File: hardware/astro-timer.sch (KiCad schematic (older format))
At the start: 25 parts, among them J1 Conn_01x02_Male, J2 AVR-ISP-6, J3 AudioJack2, SW1 SW_SPST, SW2 SW_Push, SW3 SW_Push, SW4 Rotary_Encoder_Switch, U1 ATmega328P-PU, U2 LTV-817M, Y1 Crystal

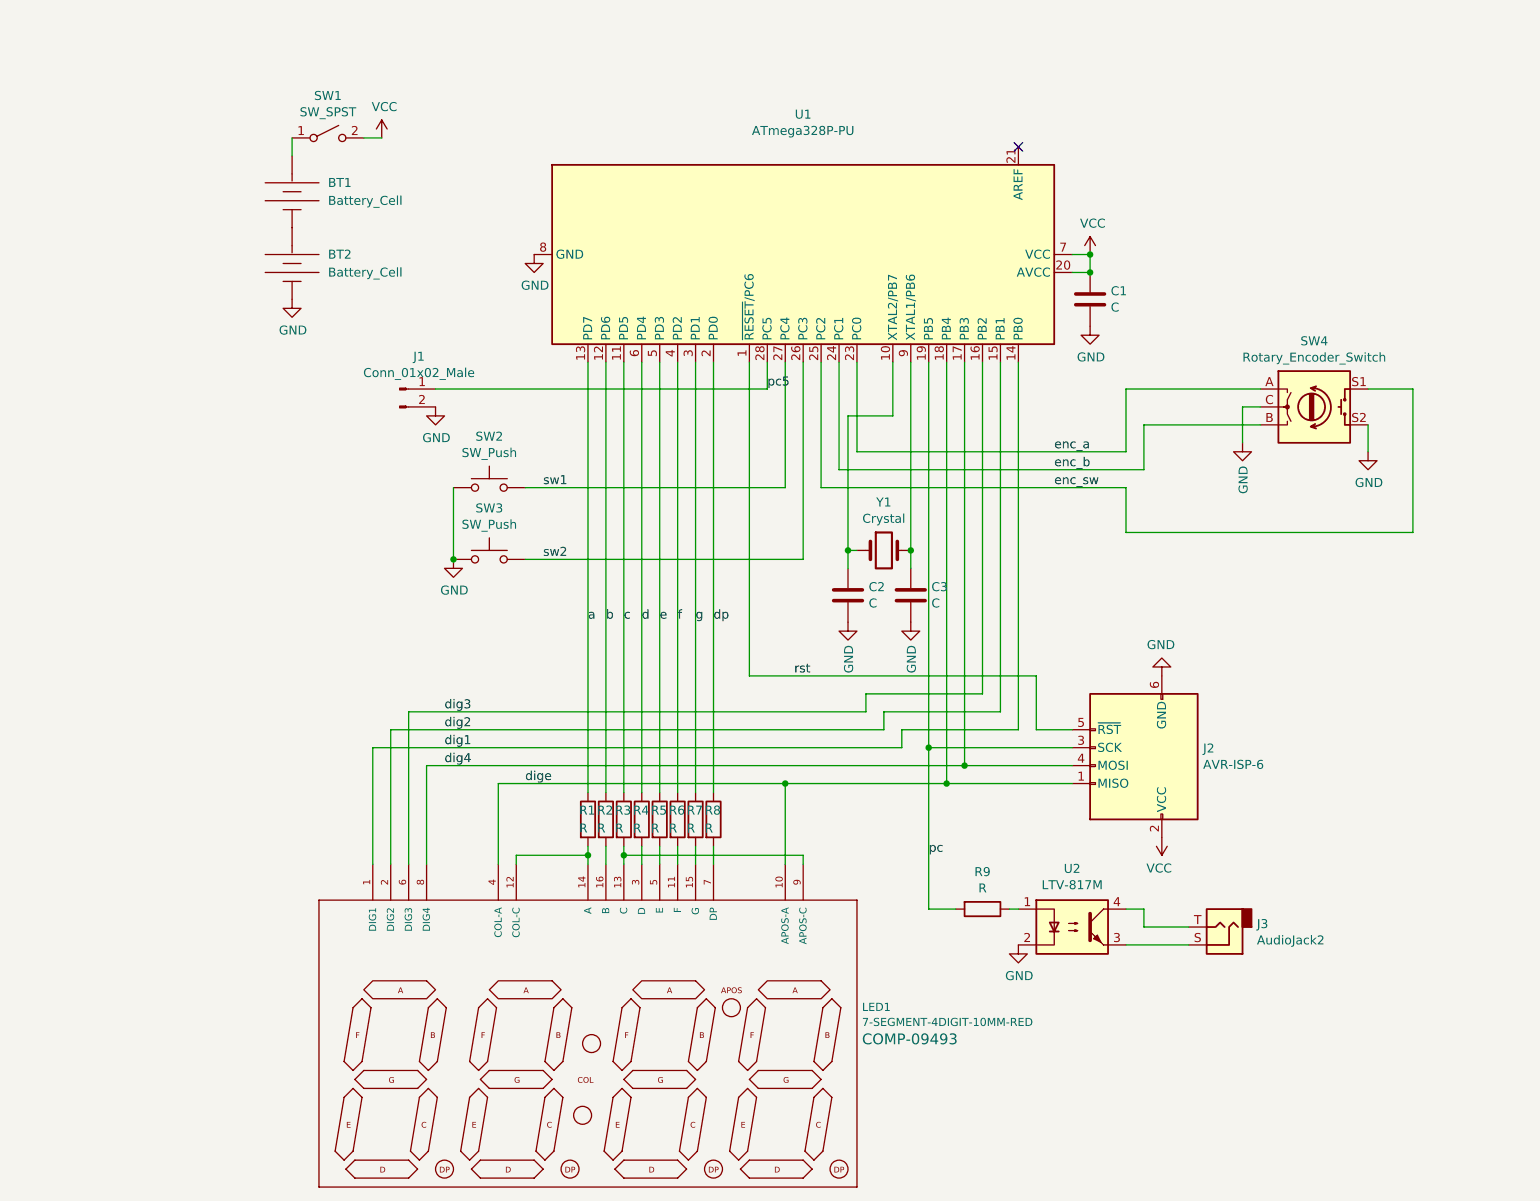
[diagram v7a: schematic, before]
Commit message: use two NPN transistors to switch both focus and shutter lines
pros:
 - lower power consumption -> better battery life. the optocoupler
   LED can easily use more power than the rest of the entire circuit
 - focus line control (a dual-channel optocoupler could do this too,
   but I don't have any on hand)
   - I don't have a particular use for this but if I want this
     thing to be generally useful, I believe Nikon cameras
     require the focus line to be asserted before the shutter
     line will release

cons:
 - transistors stick up higher than optocouplers on my board
   and it's near the encoder. this may limit knob choice
   (there's some real estate on the bottom-right of the board;
    maybe I move the transistors there?)
 - a dual-channel optocoupler would be more compact
 - the circuit is no longer electrically isolated from the
   camera
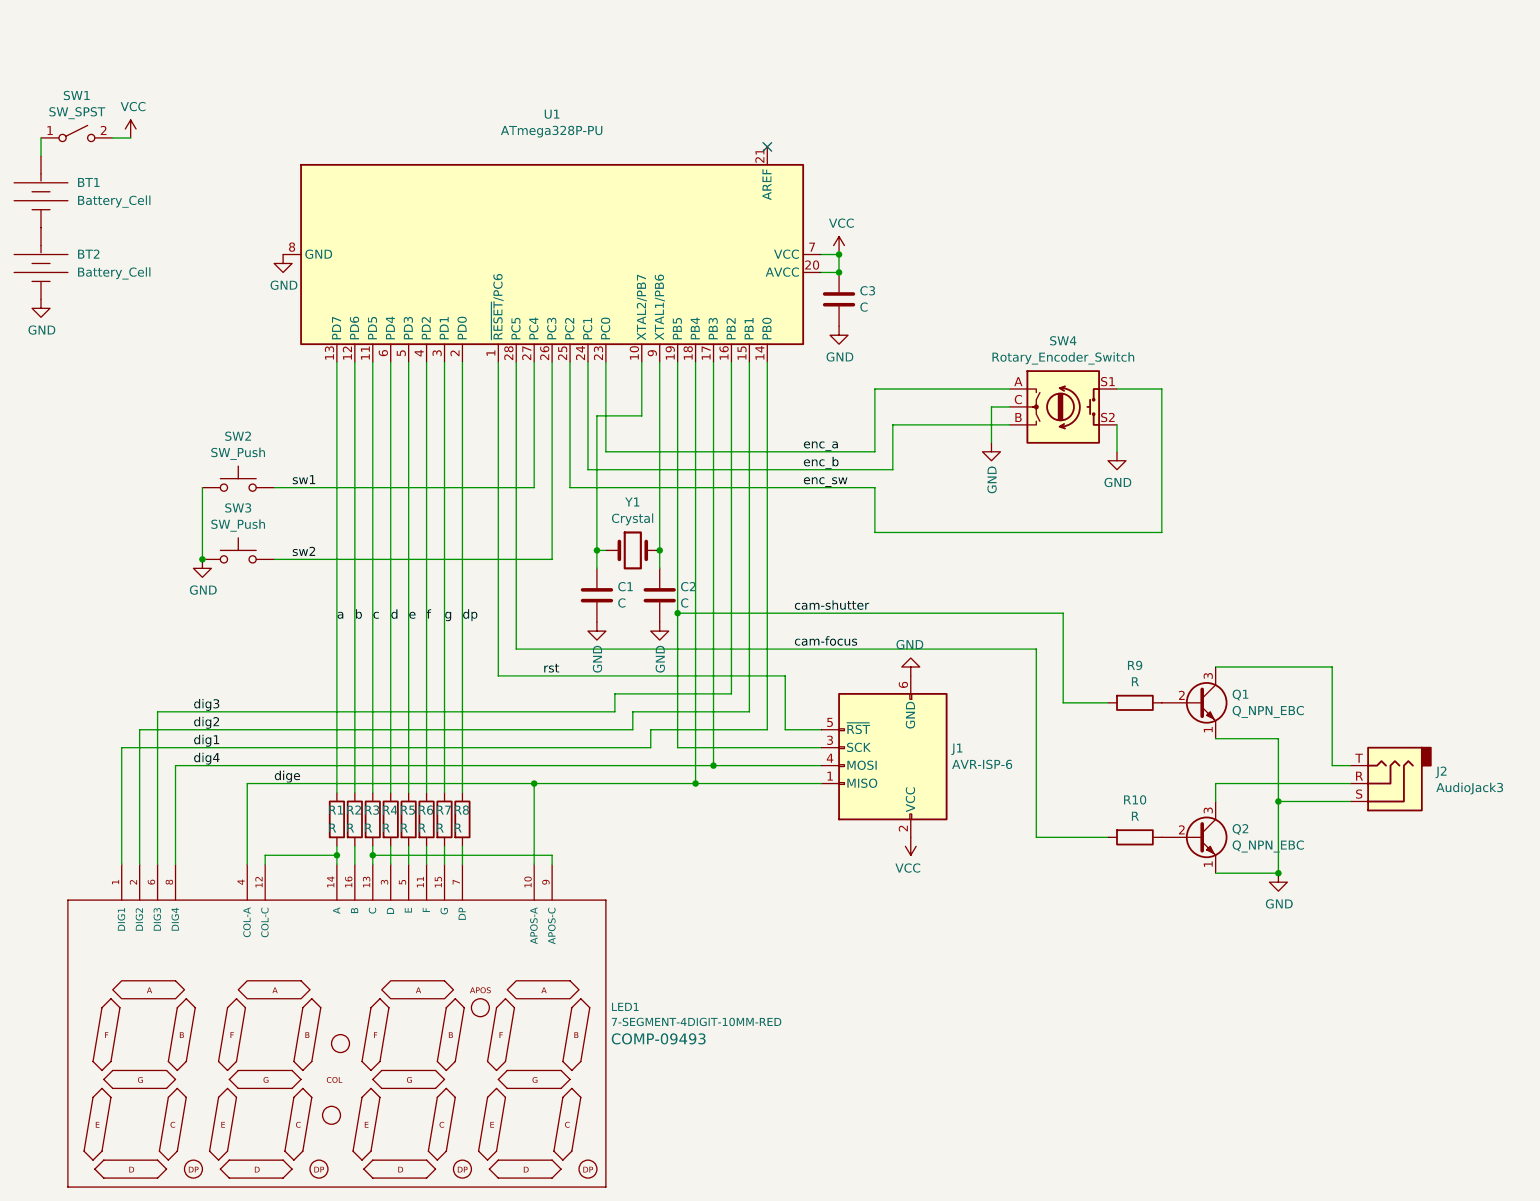
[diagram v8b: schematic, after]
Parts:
- removed J1: Conn_01x02_Male, Connector_PinHeader_2.54mm:PinHeader_1x02_P2.54mm_Vertical, symbol Connector:Conn_01x02_Male
- removed J3: AudioJack2, more_different_sj1:CUI_SJ1-2503A, symbol Connector:AudioJack2
- removed U2: LTV-817M, Package_DIP:DIP-4_W7.62mm, symbol Isolator:LTV-817M
- added J2: AudioJack3, more_different_sj1:CUI_SJ1-2503A, symbol Connector:AudioJack3
- added Q1, Q2: Q_NPN_EBC, Package_TO_SOT_THT:TO-92_Inline_Wide, symbol Device:Q_NPN_EBC
- added R10: R, Resistor_THT:R_Axial_DIN0204_L3.6mm_D1.6mm_P2.54mm_Vertical, symbol Device:R
- R9: footprint Resistor_THT:R_Axial_DIN0204_L3.6mm_D1.6mm_P7.62mm_Horizontal -> Resistor_THT:R_Axial_DIN0204_L3.6mm_D1.6mm_P2.54mm_Vertical
- renumbered C2 to C1, C3 to C2, C1 to C3, J2 to J1
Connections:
- net GND: now also J2.S, Q1.1 (E), Q2.1 (E)
- net at R9.1: now also Q1.2 (B)
- net pc renamed cam-shutter
- net pc5 renamed cam-focus
- net cam-focus: now also R10.2
- new net: J2.R, Q2.3 (C)
- new net: J2.T, Q1.3 (C)
- new net: Q2.2 (B), R10.1
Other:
- moved on the sheet: BT1, BT2, C1, C2, C3, J1, LED1, R1, R2, R3, R4, R5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
